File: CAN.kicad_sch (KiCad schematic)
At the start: 6 parts, among them U11 ZX-SH1.0-4PWT, U7 SIT1051TK/3

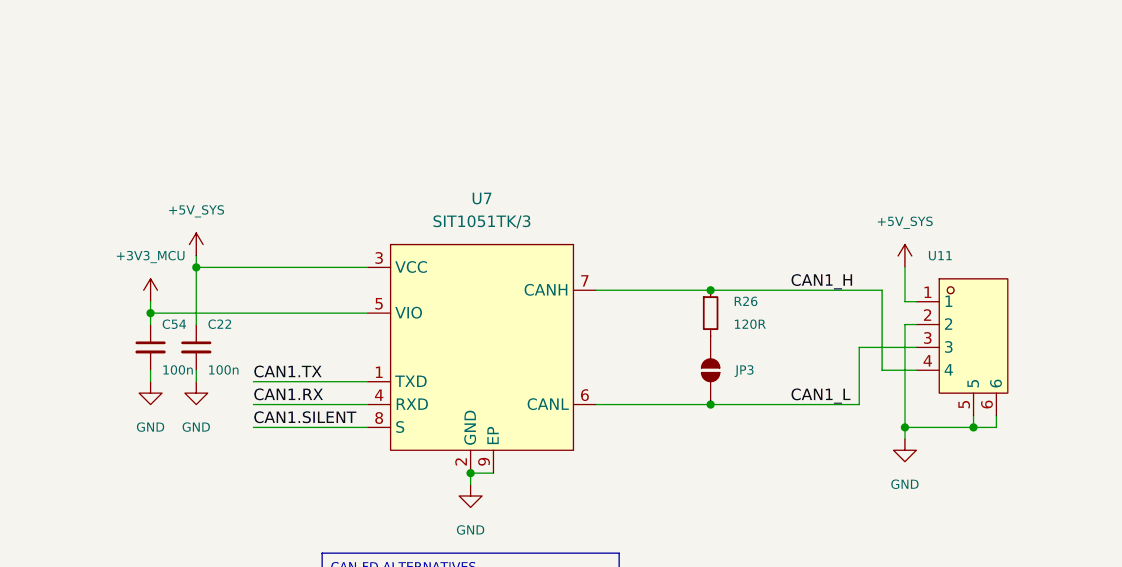
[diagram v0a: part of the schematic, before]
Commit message: grouped ICs and passives
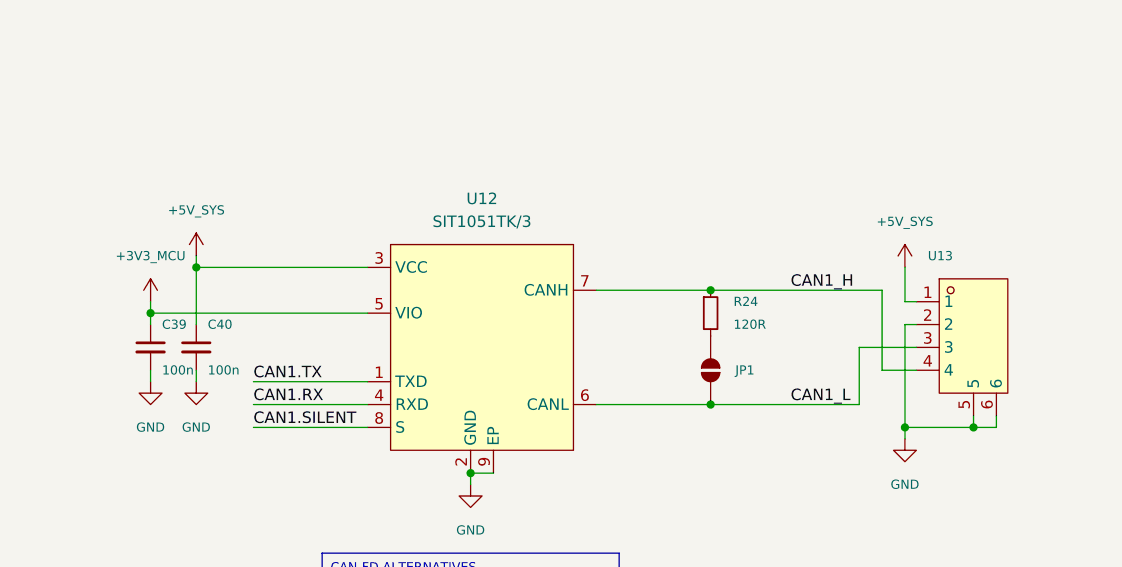
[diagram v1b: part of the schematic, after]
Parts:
- renumbered C54 to C39, C22 to C40, JP3 to JP1, R26 to R24, U7 to U12, U11 to U13
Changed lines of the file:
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@@
 		(in_pos_files yes)
 		(dnp no)
-		(property "Reference" "C22"
+		(property "Reference" "C40"
 			(at 71.12 63.5 0)
 			(show_name no)
@@
 			(project "LEVIA_H7"
 				(path "/6b768b36-fce6-4be0-9021-6d41bddc3a70/339be1e4-df07-445e-a0aa-e25cab3c571c"
-					(reference "C22")
+					(reference "C40")
 					(unit 1)
 				)
@@
 		(in_pos_files yes)
 		(dnp no)
-		(property "Reference" "JP3"
+		(property "Reference" "JP1"
 			(at 130.81 68.58 90)
 			(show_name no)
@@
 			(project "LEVIA_H7"
 				(path "/6b768b36-fce6-4be0-9021-6d41bddc3a70/339be1e4-df07-445e-a0aa-e25cab3c571c"
-					(reference "JP3")
+					(reference "JP1")
 					(unit 1)
 				)
@@
 		(dnp no)
 		(fields_autoplaced yes)
-		(property "Reference" "#PWR063"
+		(property "Reference" "#PWR084"
 			(at 69.85 59.69 0)
 			(hide yes)
@@
 			(project "LEVIA_H7"
 				(path "/6b768b36-fce6-4be0-9021-6d41bddc3a70/339be1e4-df07-445e-a0aa-e25cab3c571c"
-					(reference "#PWR063")
+					(reference "#PWR084")
 					(unit 1)
 				)
@@
 		(dnp no)
 		(fields_autoplaced yes)
-		(property "Reference" "#PWR066"
+		(property "Reference" "#PWR087"
 			(at 148.59 60.96 0)
 			(hide yes)
@@
 			(project "LEVIA_H7"
 				(path "/6b768b36-fce6-4be0-9021-6d41bddc3a70/339be1e4-df07-445e-a0aa-e25cab3c571c"
-					(reference "#PWR066")
+					(reference "#PWR087")
 					(unit 1)
 				)
@@
 		(dnp no)
 		(fields_autoplaced yes)
-		(property "Reference" "#PWR048"
+		(property "Reference" "#PWR086"
 			(at 100.33 87.63 0)
 			(hide yes)
@@
 			(project "LEVIA_H7"
 				(path "/6b768b36-fce6-4be0-9021-6d41bddc3a70/339be1e4-df07-445e-a0aa-e25cab3c571c"
-					(reference "#PWR048")
+					(reference "#PWR086")
 					(unit 1)
 				)
@@
 		(dnp no)
 		(fields_autoplaced yes)
-		(property "Reference" "#PWR088"
+		(property "Reference" "#PWR083"
 			(at 64.77 76.2 0)
 			(hide yes)
@@
 			(project "LEVIA_H7"
 				(path "/6b768b36-fce6-4be0-9021-6d41bddc3a70/339be1e4-df07-445e-a0aa-e25cab3c571c"
-					(reference "#PWR088")
+					(reference "#PWR083")
 					(unit 1)
 				)
@@
 		(in_pos_files yes)
 		(dnp no)
-		(property "Reference" "C54"
+		(property "Reference" "C39"
 			(at 66.04 63.5 0)
 			(show_name no)
@@
 			(project "LEVIA_H7"
 				(path "/6b768b36-fce6-4be0-9021-6d41bddc3a70/339be1e4-df07-445e-a0aa-e25cab3c571c"
-					(reference "C54")
+					(reference "C39")
 					(unit 1)
 				)
@@
 		(dnp no)
 		(fields_autoplaced yes)
-		(property "Reference" "#PWR047"
+		(property "Reference" "#PWR082"
 			(at 64.77 64.77 0)
 			(hide yes)
@@
 			(project "LEVIA_H7"
 				(path "/6b768b36-fce6-4be0-9021-6d41bddc3a70/339be1e4-df07-445e-a0aa-e25cab3c571c"
-					(reference "#PWR047")
+					(reference "#PWR082")
 					(unit 1)
 				)
@@
 		(dnp no)
 		(fields_autoplaced yes)
-		(property "Reference" "U7"
+		(property "Reference" "U12"
 			(at 101.6 49.53 0)
 			(show_name no)
@@
 			(project "LEVIA_H7"
 				(path "/6b768b36-fce6-4be0-9021-6d41bddc3a70/339be1e4-df07-445e-a0aa-e25cab3c571c"
-					(reference "U7")
+					(reference "U12")
 					(unit 1)
 				)
@@
 		(dnp no)
 		(fields_autoplaced yes)
-		(property "Reference" "R26"
+		(property "Reference" "R24"
 			(at 129.54 60.9599 0)
 			(show_name no)
@@
 			(project "LEVIA_H7"
 				(path "/6b768b36-fce6-4be0-9021-6d41bddc3a70/339be1e4-df07-445e-a0aa-e25cab3c571c"
-					(reference "R26")
+					(reference "R24")
 					(unit 1)
 				)
@@
 		(in_pos_files yes)
 		(dnp no)
-		(property "Reference" "U11"
+		(property "Reference" "U13"
 			(at 151.13 55.88 0)
 			(show_name no)
@@
 			(project "LEVIA_H7"
 				(path "/6b768b36-fce6-4be0-9021-6d41bddc3a70/339be1e4-df07-445e-a0aa-e25cab3c571c"
-					(reference "U11")
+					(reference "U13")
 					(unit 1)
 				)
@@
 		(dnp no)
 		(fields_autoplaced yes)
-		(property "Reference" "#PWR065"
+		(property "Reference" "#PWR088"
 			(at 148.59 82.55 0)
 			(hide yes)
@@
 			(project "LEVIA_H7"
 				(path "/6b768b36-fce6-4be0-9021-6d41bddc3a70/339be1e4-df07-445e-a0aa-e25cab3c571c"
-					(reference "#PWR065")
+					(reference "#PWR088")
 					(unit 1)
 				)
@@
 		(dnp no)
 		(fields_autoplaced yes)
-		(property "Reference" "#PWR064"
+		(property "Reference" "#PWR085"
 			(at 69.85 76.2 0)
 			(hide yes)
@@
 			(project "LEVIA_H7"
 				(path "/6b768b36-fce6-4be0-9021-6d41bddc3a70/339be1e4-df07-445e-a0aa-e25cab3c571c"
-					(reference "#PWR064")
-					(unit 1)
-				)
+					(reference "#PWR085")
+					(unit 1)
+				)
